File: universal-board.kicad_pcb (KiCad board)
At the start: 2 copper layers, 61.2 x 77.5 mm, 50 parts, among them J1 USB_C_Receptacle, J2 Conn_02x04_Odd_Even, J3 Conn_01x08, J4 CONN_WS2812, J5 CONN_I2C_GROVE, J6 CONN_UART, Q1 BSS138, SW1 SW_RESET, SW2 SW_ACK, U1 USBLC6-2SC6, U2 AMS1117-3.3, U3 CH224K, U4 USBLC6-2SC6, U5 74AHCT1G125, U6 TSOP384xx, U7 ESP32-S3-WROOM-1-N16

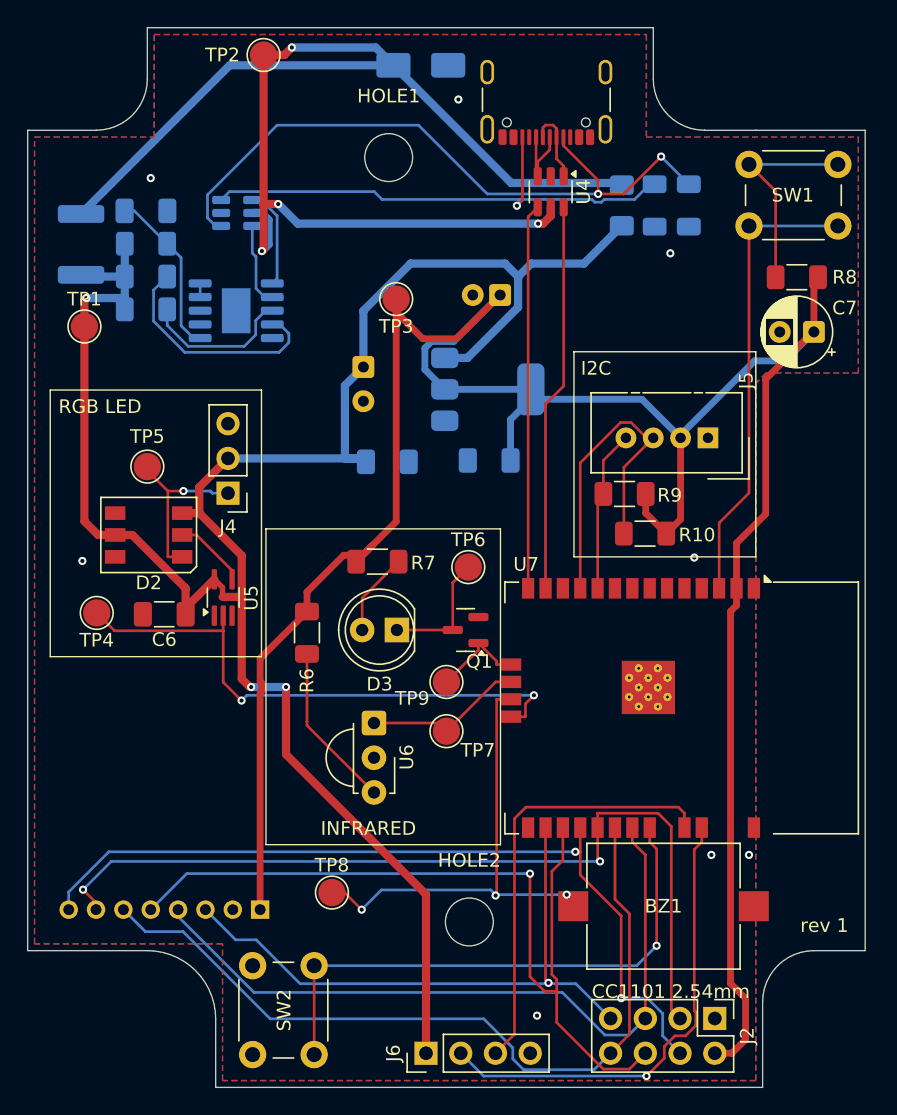
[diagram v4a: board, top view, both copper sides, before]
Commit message: - added QR code for test printing - made group labels more prominent - moved some components around to make DRC happy - connected unconnected components (!)
marked as rev 2
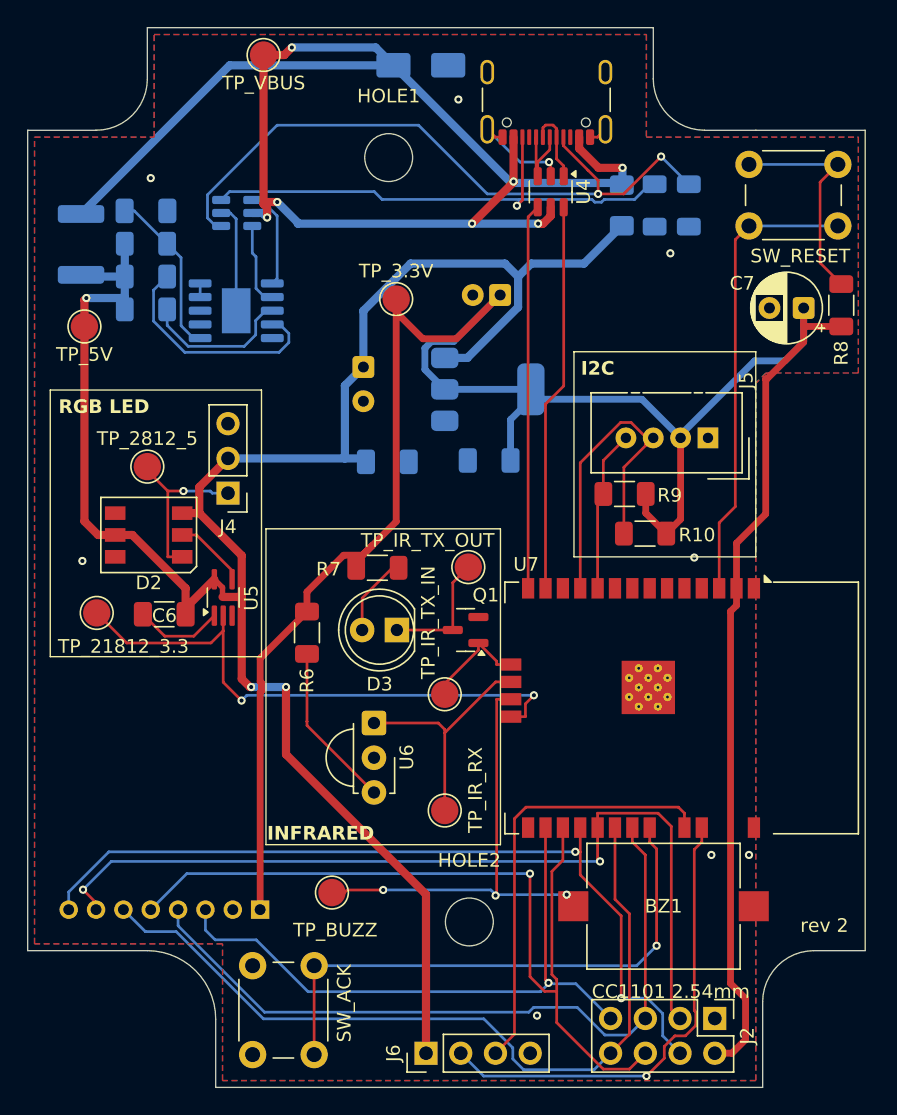
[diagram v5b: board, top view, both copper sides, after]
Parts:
- added G***: LOGO, libraries:qrcode, B.Cu at (105.2, 130.0)
- moved TP7 5.80 mm to (91.8, 127.2)
- moved R8 3.84 mm to (120.8, 90.3), turned to 90 degrees
- moved C7 1.90 mm to (118.0, 90.5)
- moved TP9 0.91 mm to (91.8, 118.8)
- moved R7 0.45 mm to (86.8, 109.5)
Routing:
- net GND: track 0.00 -> 23.8 mm, vias 8 -> 9
- net VBUS: track 98.7 -> 107.2 mm, vias 4 -> 7
- net IR_RX_OUT: track 11.8 -> 17.7 mm
- net 3.3V: track 181.6 -> 183.6 mm
- net MISO: track 44.4 -> 45.8 mm
- net 5V: track 153.0 -> 151.7 mm
- net BUZZ_IN: track 35.0 -> 33.9 mm
- net IR_TX_IN: track 7.00 -> 7.95 mm
- net Net-(SW1-A): track 15.6 -> 16.4 mm
- net WS2818_3.3V_IN: track 41.0 -> 41.7 mm
- net SCK: track 53.1 -> 53.8 mm
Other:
- board text added: "rev 2"
- board text removed: "rev 1"

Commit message: First stab at layout for rev 3
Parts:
- removed C7: 1uF, Capacitor_THT:CP_Radial_D5.0mm_P2.50mm
- removed F2: 0ZCJ0100FF2E (1A), Fuse:Fuse_1206_3216Metric_Pad1.42x1.75mm_HandSolder
- removed G***: LOGO, libraries:qrcode
- removed J3: Conn_01x08, Connector_PinHeader_2.00mm:PinHeader_1x08_P2.00mm_Vertical
- removed R10: 4.7k, Resistor_SMD:R_1206_3216Metric_Pad1.30x1.75mm_HandSolder
- removed SW1: SW_RESET, Button_Switch_THT:SW_PUSH_6mm
- removed SW2: SW_ACK, Button_Switch_THT:SW_PUSH_6mm
- removed TP1: TP_5V, TestPoint:TestPoint_Pad_D2.0mm
- removed TP2: TP_VBUS, TestPoint:TestPoint_Pad_D2.0mm
- removed TP3: TP_3.3V, TestPoint:TestPoint_Pad_D2.0mm
- removed TP4: TP_21812_3.3, TestPoint:TestPoint_Pad_D2.0mm
- removed TP5: TP_2812_5, TestPoint:TestPoint_Pad_D2.0mm
- removed TP6: TP_IR_TX_OUT, TestPoint:TestPoint_Pad_D2.0mm
- removed TP7: TP_IR_RX, TestPoint:TestPoint_Pad_D2.0mm
- removed TP8: TP_BUZZ, TestPoint:TestPoint_Pad_D2.0mm
- removed TP9: TP_IR_TX_IN, TestPoint:TestPoint_Pad_D2.0mm
- removed U5: 74AHCT1G125, Package_TO_SOT_SMD:SOT-353_SC-70-5_Handsoldering
- removed U6: TSOP384xx, OptoDevice:Vishay_MINICAST-3Pin
- removed U7: ESP32-S3-WROOM-1-N16, RF_Module:ESP32-S3-WROOM-1
- added ACK: SW_ACK, Button_Switch_THT:SW_PUSH_6mm, F.Cu at (109.3, 129.2)
- added BOOT: CONN_BOOT, Connector_PinHeader_1.00mm:PinHeader_1x02_P1.00mm_Vertical, F.Cu at (116.6, 99.7)
- added D4: LESD5D5.0CT1G, Diode_SMD:D_SOD-523, F.Cu at (79.9, 81.1)
- added D5: IR7393C, LED_THT:LED_D5.0mm_Clear, F.Cu at (96.6, 102.7)
- added D6: WS2812, LED_SMD:LED_WS2812_PLCC6_5.0x5.0mm_P1.6mm, F.Cu at (106.9, 84.3)
- added D7: WS2812B, LED_SMD:LED_WS2812B_PLCC4_5.0x5.0mm_P3.2mm, F.Cu at (114.3, 84.3)
- added J7: CONN_WS2812, Connector_PinHeader_2.54mm:PinHeader_1x03_P2.54mm_Vertical, F.Cu at (116.0, 79.5)
- added RESET: SW_RST, Button_Switch_THT:SW_PUSH_6mm, F.Cu at (109.3, 121.3)
- added TP2812_3: TP_21812_3.3, TestPoint:TestPoint_Pad_D2.0mm, F.Cu at (109.3, 92.2)
- added TP2812_5: TP_2812_5, TestPoint:TestPoint_Pad_D2.0mm, F.Cu at (115.1, 92.2)
- added TP3.3V: TP_3.3V, TestPoint:TestPoint_Pad_D2.0mm, F.Cu at (93.7, 81.0)
- added TP5V: TP_5V, TestPoint:TestPoint_Pad_D2.0mm, F.Cu at (93.6, 75.6)
- added TP_BUZZ: TP_BUZZ, TestPoint:TestPoint_Pad_D2.0mm, F.Cu at (94.0, 143.9)
- added TP_GND: TP_GND, TestPoint:TestPoint_Pad_4.0x4.0mm, F.Cu at (112.1, 144.7)
- added TP_IRTX_Q: TP_IR_TX, TestPoint:TestPoint_Pad_D2.0mm, F.Cu at (105.0, 98.5)
- added TP_IR_RX: TP_IR_RX, TestPoint:TestPoint_Pad_D2.0mm, F.Cu at (89.8, 106.7)
- added TP_IR_TX: TP_IR_TX_OUT, TestPoint:TestPoint_Pad_D2.0mm, F.Cu at (100.0, 106.8)
- C1: value 10uF -> 100nF; footprint Capacitor_THT:CP_Radial_D6.3mm_P2.50mm -> Capacitor_SMD:C_1206_3216Metric_Pad1.33x1.80mm_HandSolder; moved to F.Cu
- C2: value 100nF -> 10uF; footprint Capacitor_SMD:C_1206_3216Metric_Pad1.33x1.80mm_HandSolder -> Capacitor_SMD:CP_Elec_5x5.4; moved to F.Cu
- C3, R4, U2: moved to F.Cu
- C4: value 22uF -> 100nF; footprint Capacitor_THT:CP_Radial_D5.0mm_P2.00mm -> Capacitor_SMD:C_1206_3216Metric_Pad1.33x1.80mm_HandSolder; moved to F.Cu
- C5: value 1uF -> 22uF; footprint Capacitor_SMD:C_1206_3216Metric_Pad1.33x1.80mm_HandSolder -> Capacitor_SMD:CP_Elec_5x5.4; moved to F.Cu
- D1: value SMAJ5.0CA -> LESD5D5.0CT1G; footprint Diode_SMD:D_SMA -> Diode_SMD:D_SOD-523; moved to F.Cu
- D2: value WS2812 -> LESD5D5.0CT1G; footprint LED_SMD:LED_WS2812_PLCC6_5.0x5.0mm_P1.6mm -> Diode_SMD:D_SOD-523
- D3: value LL-503SIRC2H-1BE -> LESD5D5.0CT1G; footprint LED_THT:LED_D5.0mm_Clear -> Diode_SMD:D_SOD-523
- F1: value PTS18126V300 (3A) -> 0ZCJ0100FF2E (1A); footprint Fuse:Fuse_1812_4532Metric_Pad1.30x3.40mm_HandSolder -> Fuse:Fuse_1206_3216Metric_Pad1.42x1.75mm_HandSolder; moved to F.Cu
- HOLE1, HOLE2: value MountingHole_3.5mm -> MountingHole_4mm; footprint MountingHole:MountingHole_3.5mm -> MountingHole:MountingHole_4mm
- J1: footprint Connector_USB:USB_C_Receptacle_GCT_USB4105-xx-A_16P_TopMnt_Horizontal -> Connector_USB:USB_C_Receptacle_G-Switch_GT-USB-7010ASV
- J2: value Conn_02x04_Odd_Even -> CONN_I2C_GROVE; footprint Connector_PinHeader_2.54mm:PinHeader_2x04_P2.54mm_Vertical -> Connector:NS-Tech_Grove_1x04_P2mm_Vertical
- J4: value CONN_WS2812 -> CONN_CC1101_2; footprint Connector_PinHeader_2.54mm:PinHeader_1x03_P2.54mm_Vertical -> Connector_PinHeader_2.54mm:PinHeader_2x04_P2.54mm_Vertical
- J5: value CONN_I2C_GROVE -> CONN_CC1101_1; footprint Connector:NS-Tech_Grove_1x04_P2mm_Vertical -> Connector_PinHeader_2.00mm:PinHeader_1x08_P2.00mm_Vertical
- R1: value 10k -> 4.7k; moved to F.Cu
- R2: value 1k -> 4.7k; moved to F.Cu
- R3: value 10k -> 5.1k; moved to F.Cu
- R5: value 5.1k -> 10k; moved to F.Cu
- R6: value 100 -> 22
- R8: value 10k -> 100
- R9: value 4.7k -> 22
- U1: value USBLC6-2SC6 -> ESP32-S2-MINI-2; footprint Package_TO_SOT_SMD:SOT-23-6 -> PCM_Espressif:ESP32-S2-MINI-1; moved to F.Cu
- U3: value CH224K -> TSOP384xx; footprint Package_SO:SSOP-10-1EP_3.9x4.9mm_P1mm_EP2.1x3.3mm -> OptoDevice:Vishay_MINICAST-3Pin; moved to F.Cu
- U4: value USBLC6-2SC6 -> 74AHCT1G125; footprint Package_TO_SOT_SMD:SOT-23-6 -> Package_TO_SOT_SMD:SOT-353_SC-70-5
- moved R2 66.9 mm to (108.3, 140.5), turned to 180 degrees
- moved R1 59.9 mm to (108.3, 136.5), turned to 0 degrees
- moved C6 47.9 mm to (105.9, 79.8), turned to 0 degrees
- moved U1 42.2 mm to (110.2, 109.0), turned to -90 degrees
- moved J5 41.8 mm to (87.4, 134.5), turned to 180 degrees
- moved R5 36.3 mm to (114.9, 118.5), turned to 180 degrees
- moved D3 35.3 mm to (75.6, 81.1), turned to 0 degrees
- moved D1 34.4 mm to (112.3, 98.9)
- moved R8 33.9 mm to (88.0, 99.0), turned to -90 degrees
- moved C5 32.2 mm to (100.5, 93.5)
- moved J4 31.2 mm to (68.1, 134.3), turned to 90 degrees
- moved R6 30.5 mm to (75.7, 84.3)
- moved J6 29.4 mm to (105.2, 119.6), turned to 0 degrees
- moved D2 28.0 mm to (87.7, 85.3), turned to 90 degrees
- moved C1 27.7 mm to (113.5, 96.0), turned to 0 degrees
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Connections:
- BZ1 pad 1: BUZZ_IN -> BUZZ_OUT
- C1 pad 1: 5V -> 3.3V
- C3 pad 1: 3.3V -> 5V
- C5 pad 1: Net-(U3-VDD) -> 3.3V
- D1 pad 2: VBUS -> 3.3V
- D2 pad 1: Net-(D2-DOUT) -> GND
- D2 pad 2: Net-(D2-DIN) -> 5V
- D3 pad 1: Net-(D3-K) -> GND
- D3 pad 2: Net-(D3-A) -> Net-(D3-A2)
- F1 pad 1: VBUS -> Net-(F1-Pad1)
- J1 pad A4: VBUS -> Net-(F1-Pad1)
- J1 pad A5: CC1 -> Net-(J1-CC1)
- J1 pad A6: Net-(J1-D+-PadA6) -> Net-(D4-A2)
- J1 pad A7: Net-(J1-D--PadA7) -> Net-(D3-A2)
- J1 pad A9: VBUS -> Net-(F1-Pad1)
- J1 pad B5: CC2 -> Net-(J1-CC2)
- J1 pad B6: Net-(J1-D+-PadA6) -> Net-(D4-A2)
- J1 pad B7: Net-(J1-D--PadA7) -> Net-(D3-A2)
- J2 pad 1: GND -> Net-(J2-Pin_1)
- J2 pad 2: 3.3V -> Net-(J2-Pin_2)
- J2 pad 3: GDO0 -> 3.3V
- J2 pad 4: CSN -> GND
- J4 pad 1: Net-(D2-DOUT) -> GND
- J4 pad 2: 5V -> 3.3V
- J4 pad 3: GND -> GDO0
- J5 pad 1: GND -> 3.3V
- J5 pad 2: 3.3V -> GND
- J5 pad 3: Net-(J5-Pin_3) -> MISO
- J5 pad 4: Net-(J5-Pin_4) -> SCK
- Q1 pad 3: Net-(D3-K) -> Net-(D5-K)
- R1 pad 1: Net-(U3-VBUS) -> Net-(J2-Pin_1)
- R1 pad 2: 5V -> 3.3V
- R2 pad 1: 5V -> 3.3V
- R2 pad 2: Net-(U3-VDD) -> Net-(J2-Pin_2)
- R3 pad 1: 5V -> GND
- R3 pad 2: Net-(U3-CFG1) -> Net-(J1-CC2)
- R4 pad 1: GND -> Net-(J1-CC1)
- R4 pad 2: CC1 -> GND
- R5 pad 1: CC2 -> Net-(SW1-B)
- R5 pad 2: GND -> 3.3V
- R6 pad 1: 3.3V -> Net-(D3-A2)
- R6 pad 2: Net-(U6-Vs) -> USB-
- R7 pad 1: 3.3V -> Net-(D4-A2)
- R7 pad 2: Net-(D3-A) -> USB+
- R8 pad 2: Net-(SW1-A) -> Net-(U3-Vs)
- R9 pad 2: Net-(J5-Pin_4) -> Net-(D5-A)
- U1 pad 1: CC1 -> GND
- U1 pad 3: CC2 -> 3.3V
- U1 pad 4: Net-(U3-CC2) -> Net-(J3-Pin_1)
- U3 pad 1: Net-(U3-VDD) -> IR_RX_OUT
- U3 pad 3: GND -> Net-(U3-Vs)
- U4 pad 1: Net-(J1-D--PadA7) -> GND
- U4 pad 2: GND -> WS2818_3.3V_OUT
- U4 pad 3: Net-(J1-D+-PadA6) -> GND
- U4 pad 4: USB+ -> Net-(D6-DIN)
- U4 pad 5: VBUS -> 5V
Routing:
- net GND: track 23.8 -> 251.4 mm, vias 9 -> 0
- net VBUS: track 107.2 -> 0.00 mm, vias 7 -> 0
- net 5V: track 151.7 -> 65.6 mm, vias 3 -> 0
- net BUZZ_OUT: track 0.00 -> 51.7 mm
- net CC1: track 49.5 -> 0.00 mm, vias 2 -> 0
- net WS2818_3.3V_IN: track 41.7 -> 0.00 mm, vias 2 -> 0
- net CC2: track 38.5 -> 0.00 mm, vias 1 -> 0
- net 3.3V: track 183.6 -> 147.5 mm, vias 0 -> 2
- net BUZZ_IN: track 33.9 -> 0.00 mm, vias 3 -> 0
- net Net-(J2-Pin_2): track 0.00 -> 31.9 mm
- net Net-(F1-Pad1): track 0.00 -> 29.4 mm, vias 0 -> 2
- net UART_TX: track 34.7 -> 8.52 mm, vias 1 -> 0
- net Net-(J2-Pin_1): track 0.00 -> 25.5 mm
- net Net-(D6-DIN): track 0.00 -> 24.8 mm
- net Net-(J5-Pin_3): track 23.9 -> 0.00 mm
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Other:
- board text added: "esphome-universal-board rev 3"
- board text removed: "1A PSU"
- board text removed: "3A PSU"
- board text removed: "5v -> 3.3v"
- board text removed: "CC1101 2.54mm"
- board text removed: "CC1101 2mm"
- board text removed: "I2C"
- board text removed: "INFRARED"
- board text removed: "RGB LED"
- board text removed: "github.com/jasiek/esphome-universal-board"
- board text removed: "rev 2"

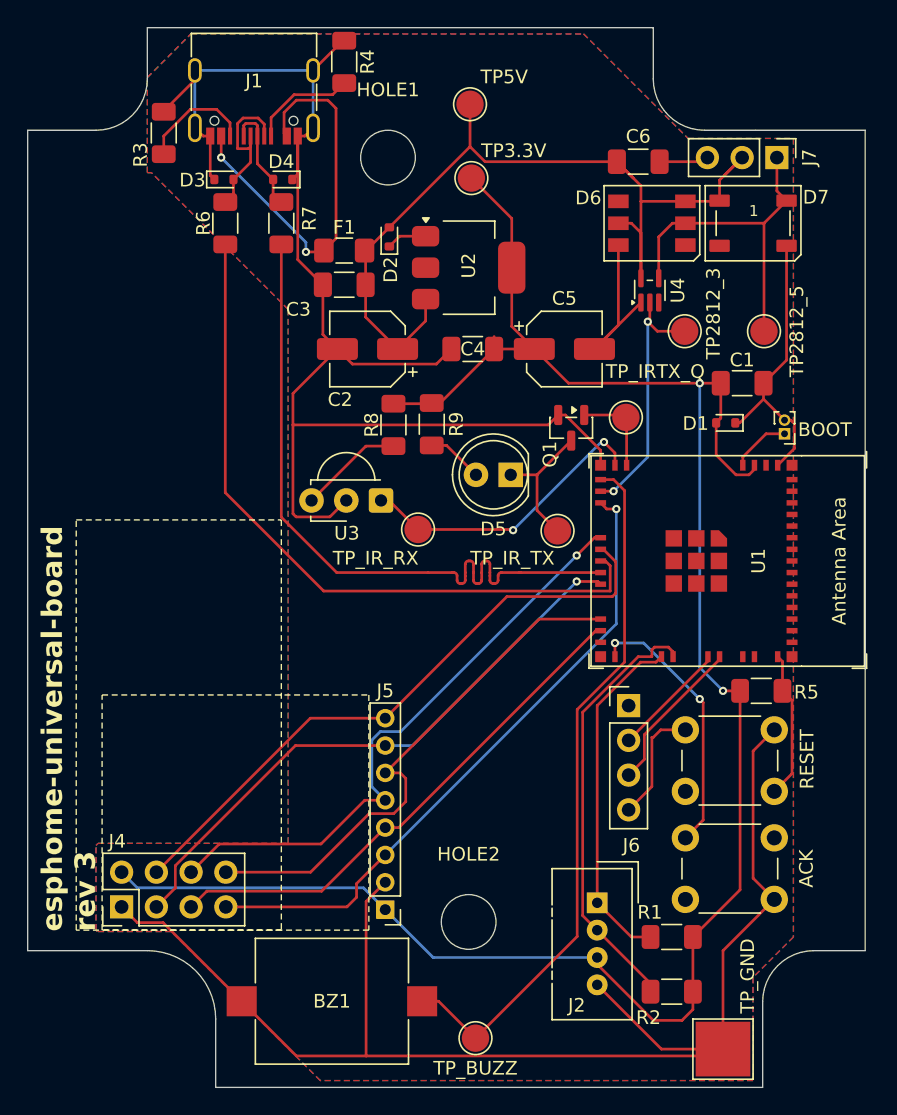
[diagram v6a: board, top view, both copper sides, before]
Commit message: Routing done, pending DRC
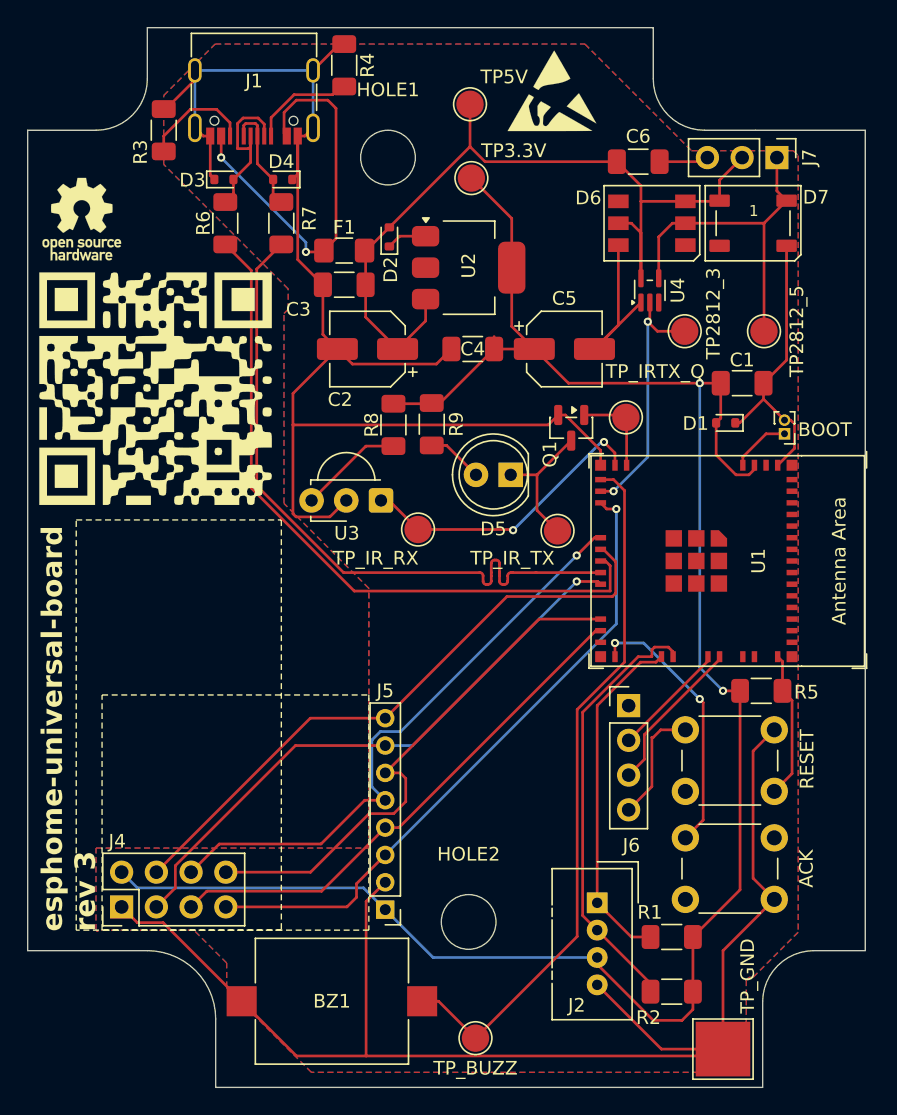
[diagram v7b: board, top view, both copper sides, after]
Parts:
- added G***: https://github.com/jasiek/esphome-universal-board, libraries:qrcode, F.Cu at (70.6, 96.4)
- added REF**: OSHW-Logo_5.7x6mm_SilkScreen, Symbol:OSHW-Logo_5.7x6mm_SilkScreen, F.Cu at (65.2, 84.0)
- added REF**: ESD-Logo_6.6x6mm_SilkScreen, Symbol:ESD-Logo_6.6x6mm_SilkScreen, F.Cu at (99.6, 74.6)
- moved R4 0.25 mm to (84.4, 72.8)
- moved R3 0.20 mm to (71.2, 77.5)
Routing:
- net 5V: track 65.6 -> 62.0 mm
- net USB-: track 52.0 -> 50.7 mm
- net USB+: track 51.8 -> 50.6 mm
